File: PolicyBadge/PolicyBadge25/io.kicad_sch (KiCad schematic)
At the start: 24 parts, among them J2 Conn_01x06_Pin, Q1 2N7002, SW1 SW_Push, SW2 SW_Push, SW4 SW_Push, SW5 SW_Push, U4 TCA9555PWR

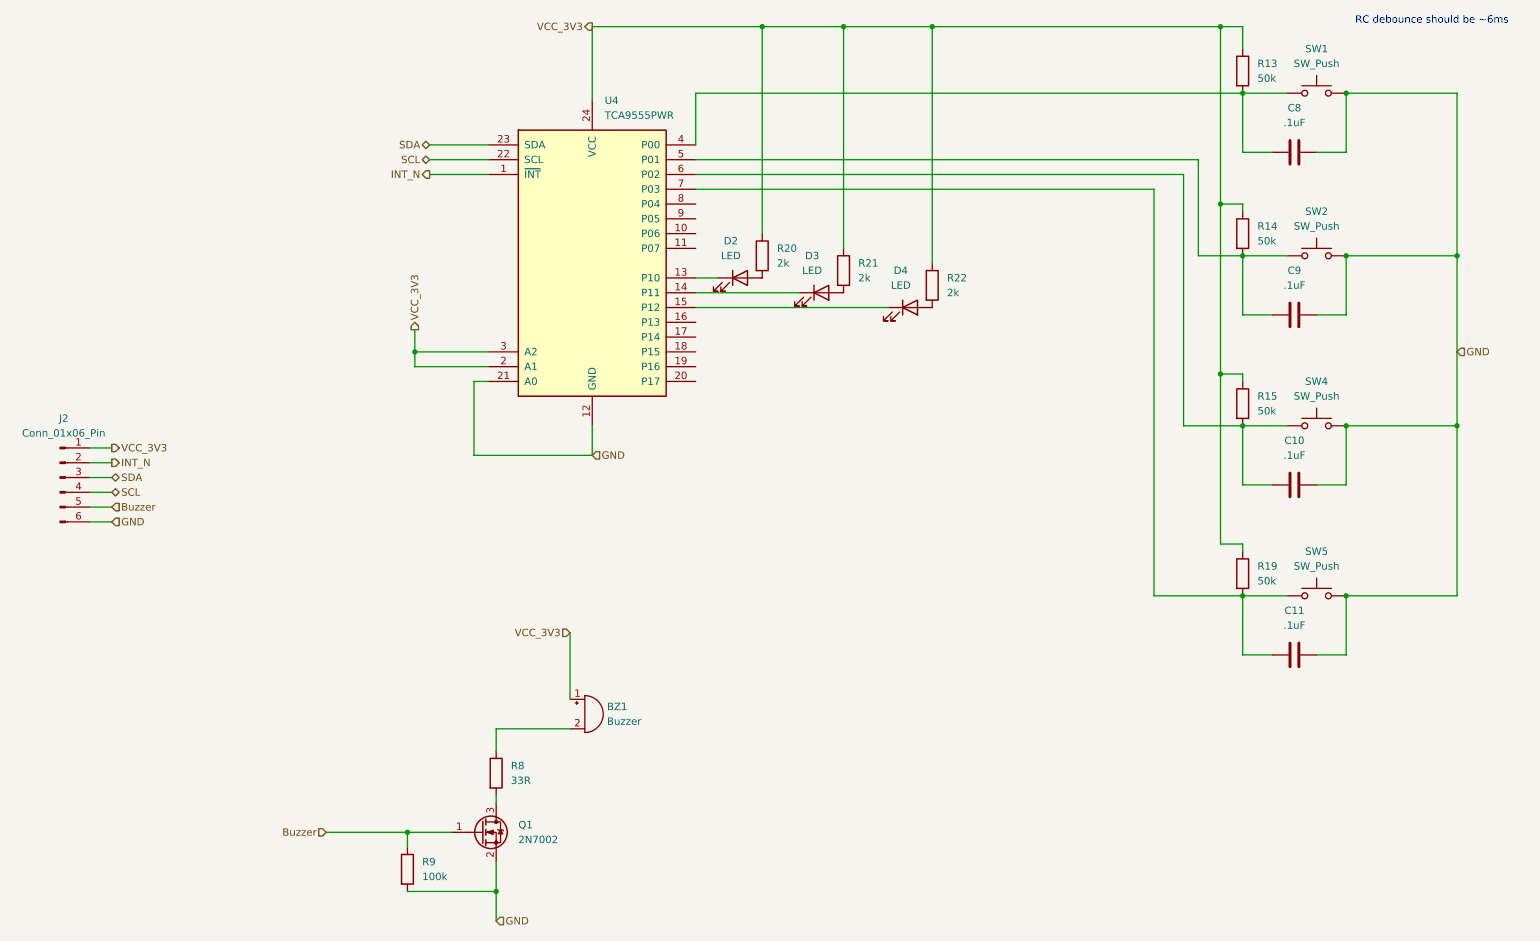
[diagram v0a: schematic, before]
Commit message: update with jlcpcb parts
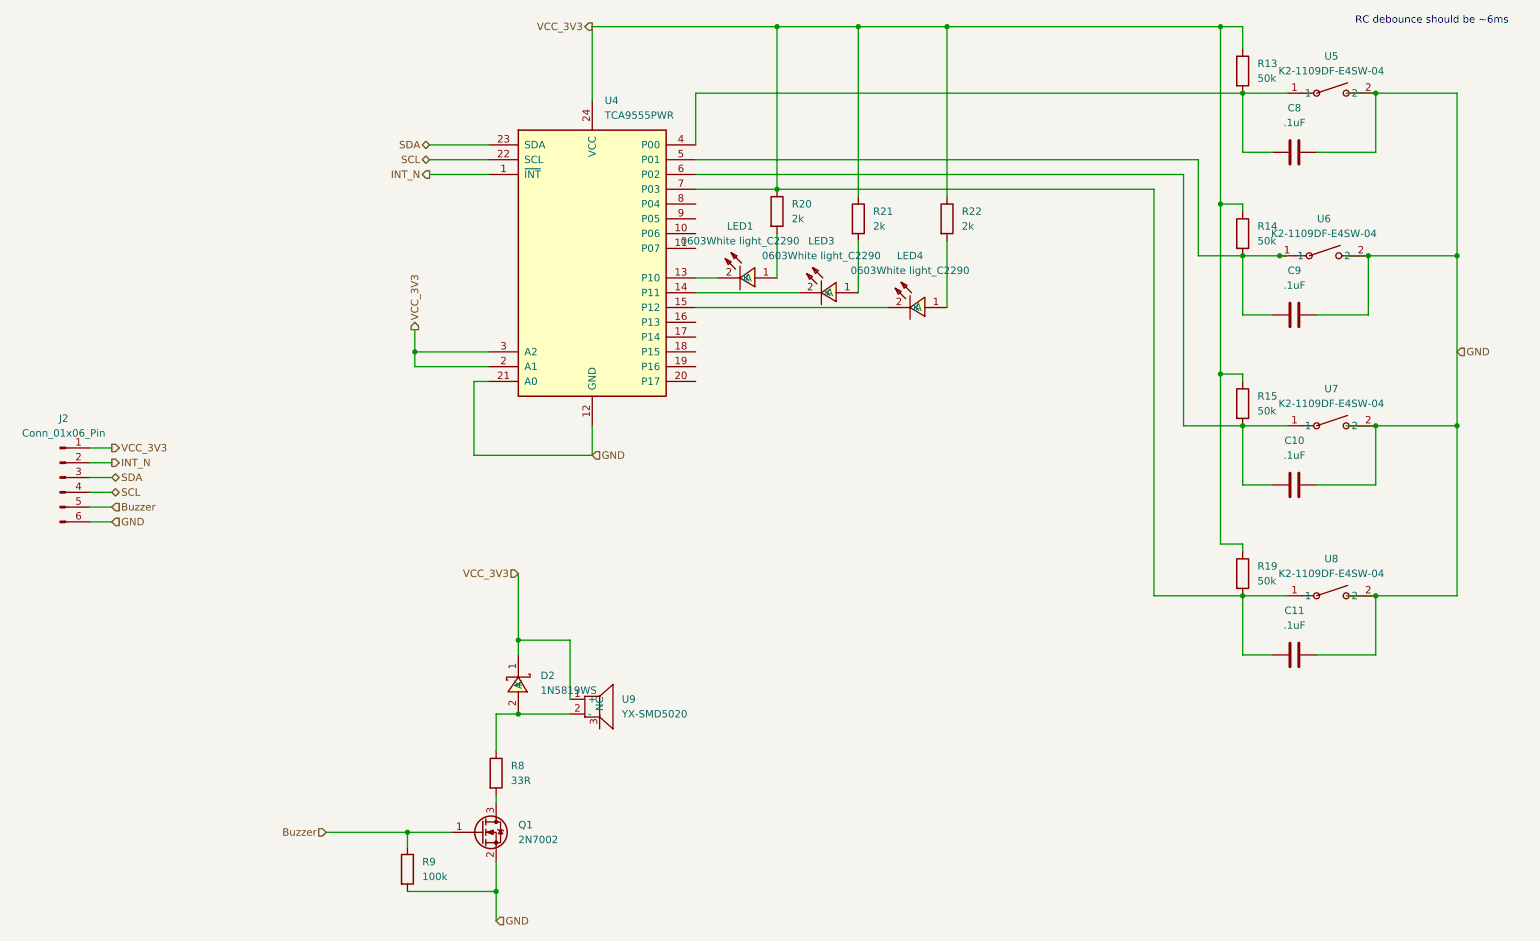
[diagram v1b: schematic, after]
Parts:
- removed BZ1: Buzzer, symbol Device:Buzzer
- removed D2, D3, D4: LED, symbol Device:LED
- removed SW1, SW2, SW4, SW5: SW_Push, symbol Switch:SW_Push
- added D2: 1N5819WS, easyeda2kicad:SOD-323_L1.8-W1.3-LS2.5-RD, symbol easyeda2kicad:1N5819WS
- added LED1, LED3, LED4: 0603White light_C2290, easyeda2kicad:LED0603-R-RD_WHITE, symbol easyeda2kicad:0603Whitelight_C2290
- added U5, U6, U7, U8: K2-1109DF-E4SW-04, easyeda2kicad:SW-TH_HRO_K2-1109DF-EXXW-XX, symbol easyeda2kicad:K2-1109DF-E4SW-04
- added U9: YX-SMD5020, easyeda2kicad:BUZ-SMD_3P_L5.0-W5.0-P3.50-TL, symbol easyeda2kicad:YX-SMD5020
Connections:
- net GND: now also U5.2, U6.2, U7.2, U8.2
- net VCC_3V3: now also C11.1, R19.2, U4.7 (P03), D2.1 (K), U8.1, U9.1 (+)
- net at U4.13 (P10): now also LED1.2 (K)
- net at U4.14 (P11): now also LED3.2 (K)
- net at U4.15 (P12): now also LED4.2 (K)
- net at C8.1, R13.2, U4.4 (P00): now also U5.1
- net at C9.1, R14.2, U4.5 (P01): now also U6.1
- net at C10.1, R15.2, U4.6 (P02): now also U7.1
- net at R8.1: now also D2.2 (A), U9.2 (-)
- net at R21.2: now also LED3.1 (A)
- net at R20.2: now also LED1.1 (A)
- net at R22.2: now also LED4.1 (A)
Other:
- moved on the sheet: R20, R21, R22
